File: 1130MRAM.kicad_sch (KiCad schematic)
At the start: 123 parts, among them J1 Screw_Terminal_01x03, J1A09 SLTpad, J1A11 SLTpad, K1E09 SLTpad, K1E11 SLTpad, M1A09 SLTpad, M1A11 SLTpad, M1C09 SLTpad, M1D09 SLTpad, M1E09 SLTpad, M1E11 SLTpad, Q1 IRF540N, SW1 SLTpad, U1 MR0A16AYS35, U10 74LCX38, U11 74LCX38, U12 SN74LVC1G123DCUR, U13 SN74LVC1G123DCUR, U14 74HC00, U15 74LS86, U16 74LS86, U17 74LS86, U18 74LS86, U2 SN74LV240APWR, U3 SN74LV240APWR, U4 LDL1117, U5 SN74LVC1G123DCUR, U6 SN74LVC1G123DCUR, U7 74LCX38, U8 74LCX38, U9 74LCX38

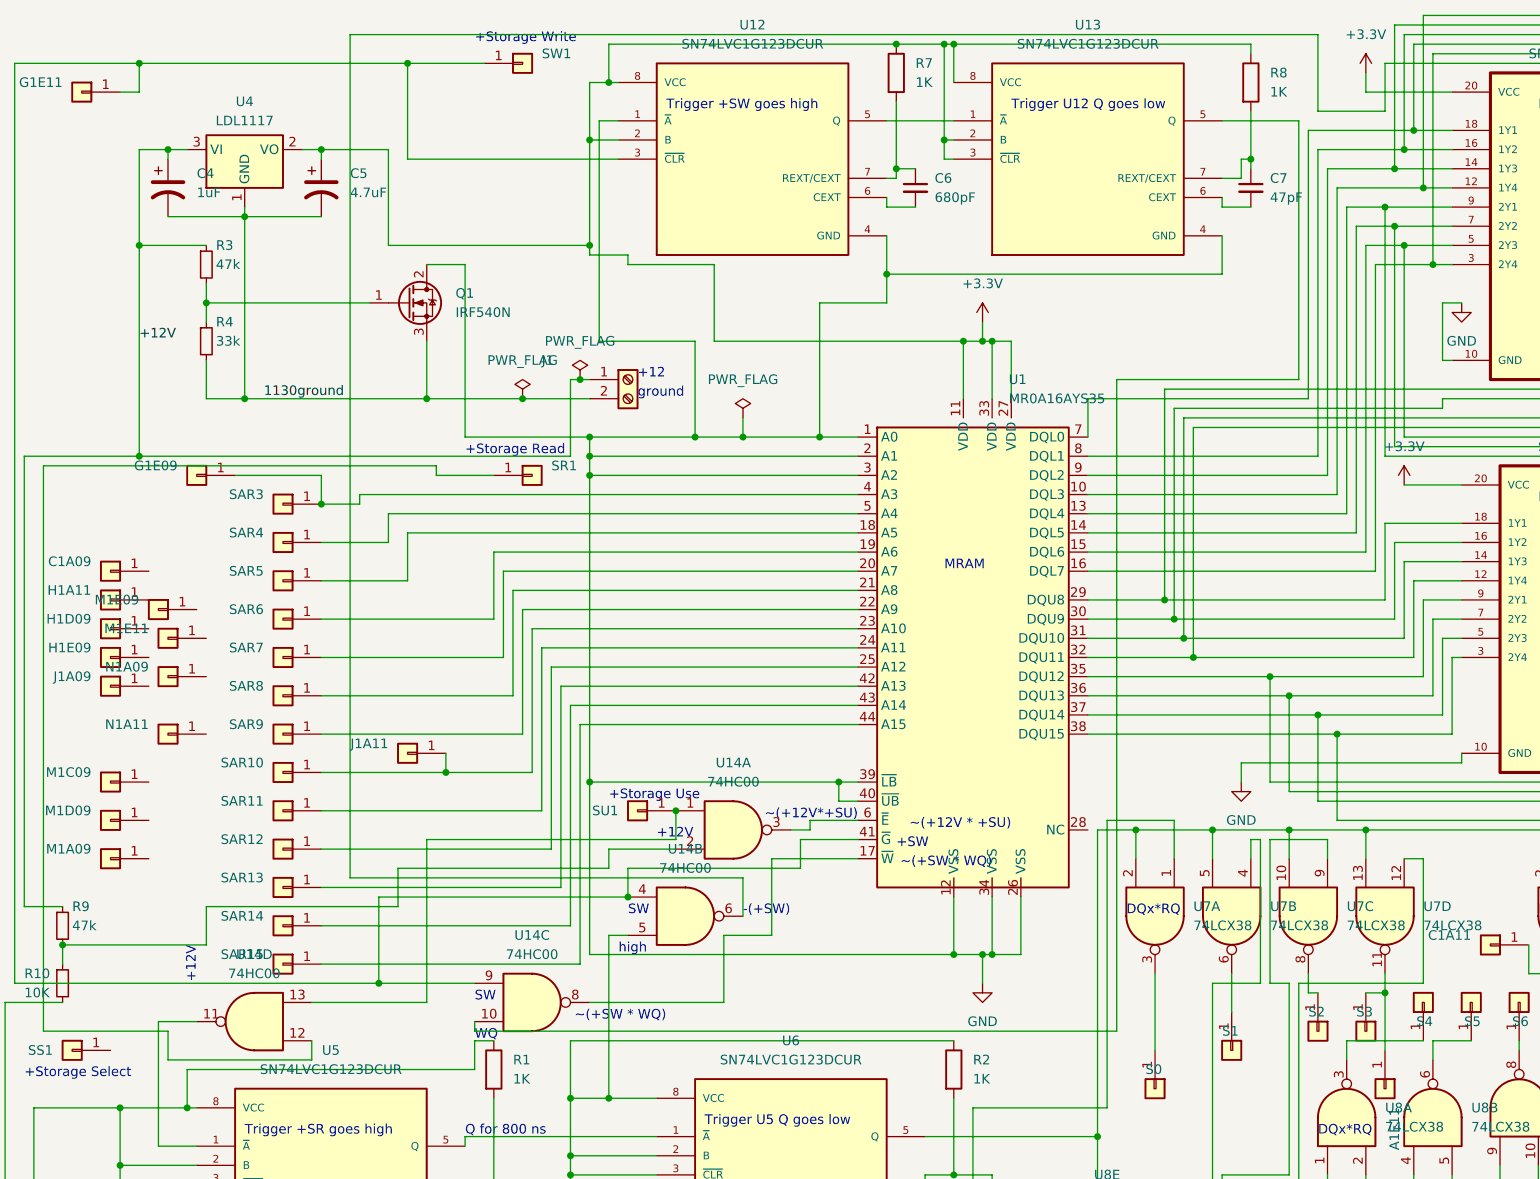
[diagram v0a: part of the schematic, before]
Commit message: Newest version of the PCB
based on testing with the 1130, the PCB was modified substantially
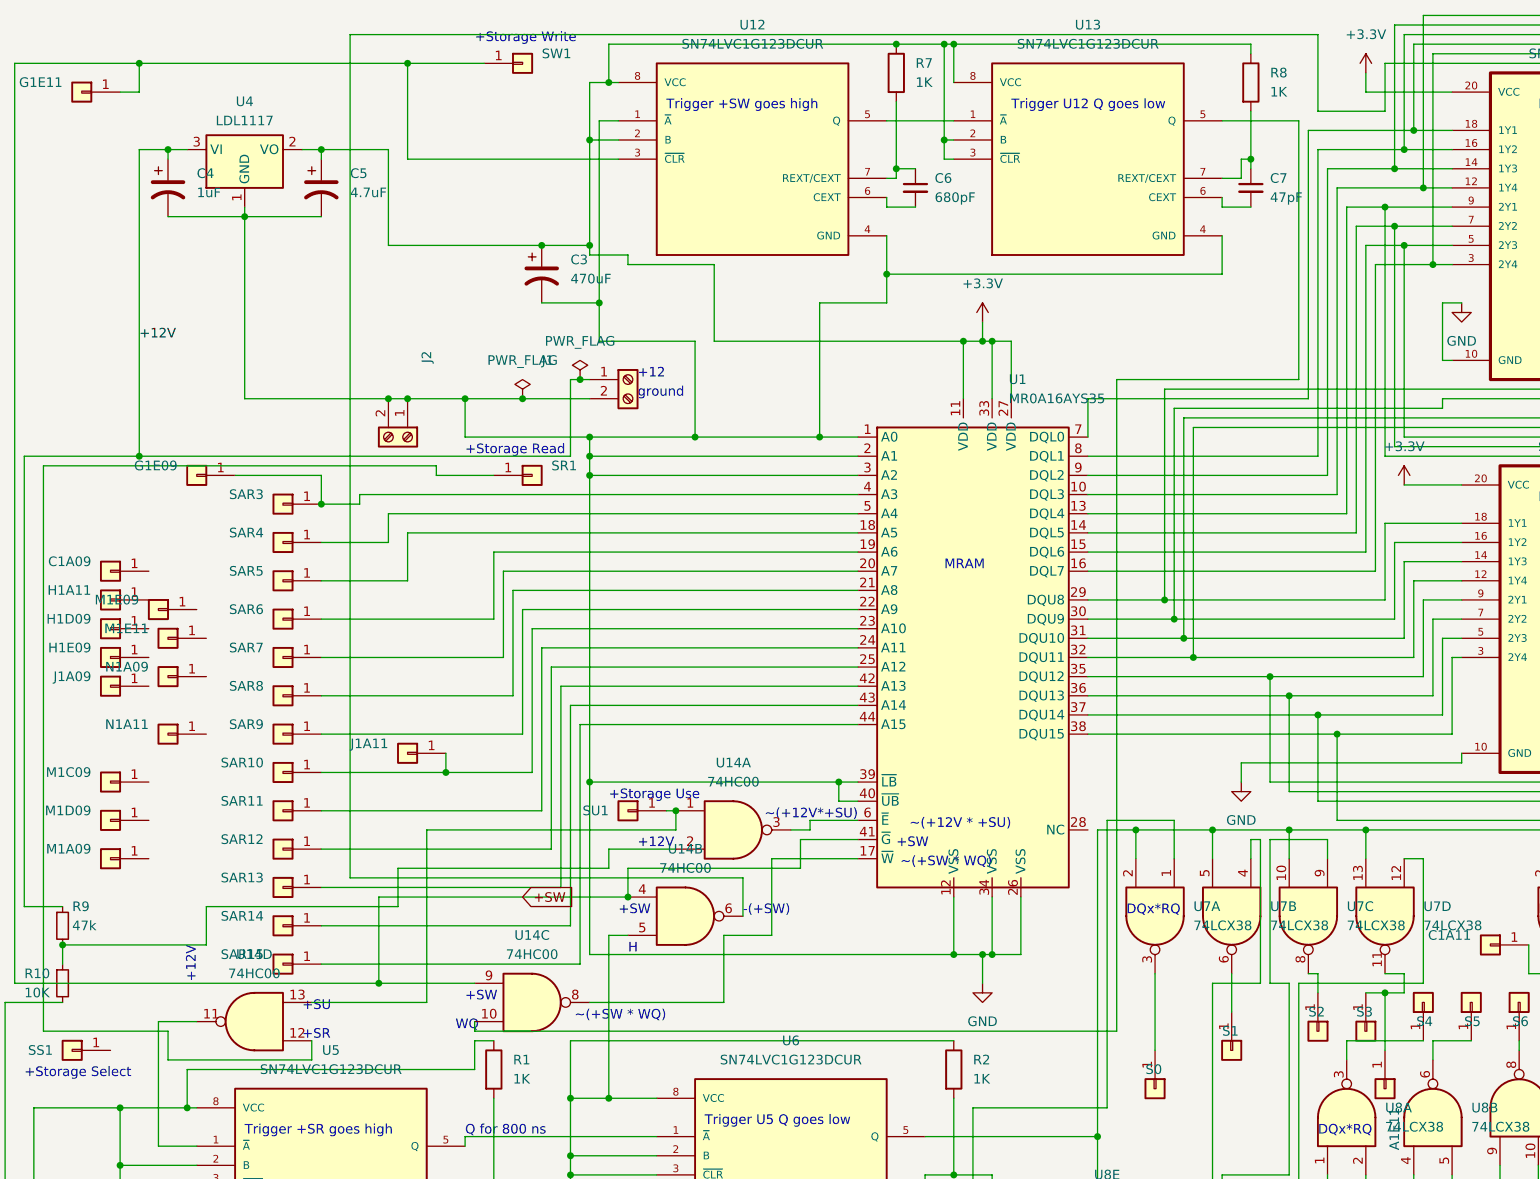
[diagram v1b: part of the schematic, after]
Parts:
- removed Q1: IRF540N, Package_TO_SOT_SMD:TO-263-2, symbol Transistor_FET:IRF540N
- removed R3: 47k, Resistor_SMD:R_0805_2012Metric, symbol Device:R_Small
- removed R4: 33k, Resistor_SMD:R_0805_2012Metric, symbol Device:R_Small
- added C3: 470uF, Capacitor_Tantalum_SMD:CP_EIA-7343-30_AVX-N, symbol Device:C_Polarized_US
- added J2: Screw_Terminal_01x03, Connector_Phoenix_MC_HighVoltage:PhoenixContact_MCV_1,5_2-G-5.08_1x02_P5.08mm_Vertical, symbol Connector:Screw_Terminal_01x02
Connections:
- net 1130ground is gone; now on net GND: C4.2, C5.2, J1.2 (Pin_2), U4.1 (GND)
- net +3.3V: now also C3.1
- net GND: now also C3.2, J2.1 (Pin_1), J2.2 (Pin_2)
- net +SW: now reaches G1E11.1 (Pin_1), SW1.1 (Pin_1), U1.41 (~{G}), U12.3 (~{CLR}), U14.4, U14.9
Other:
- note added: "+SR"
- note added: "+SU"
- note added: "H"
- note removed: "SW"
- note removed: "high"
- moved on the sheet: SU1

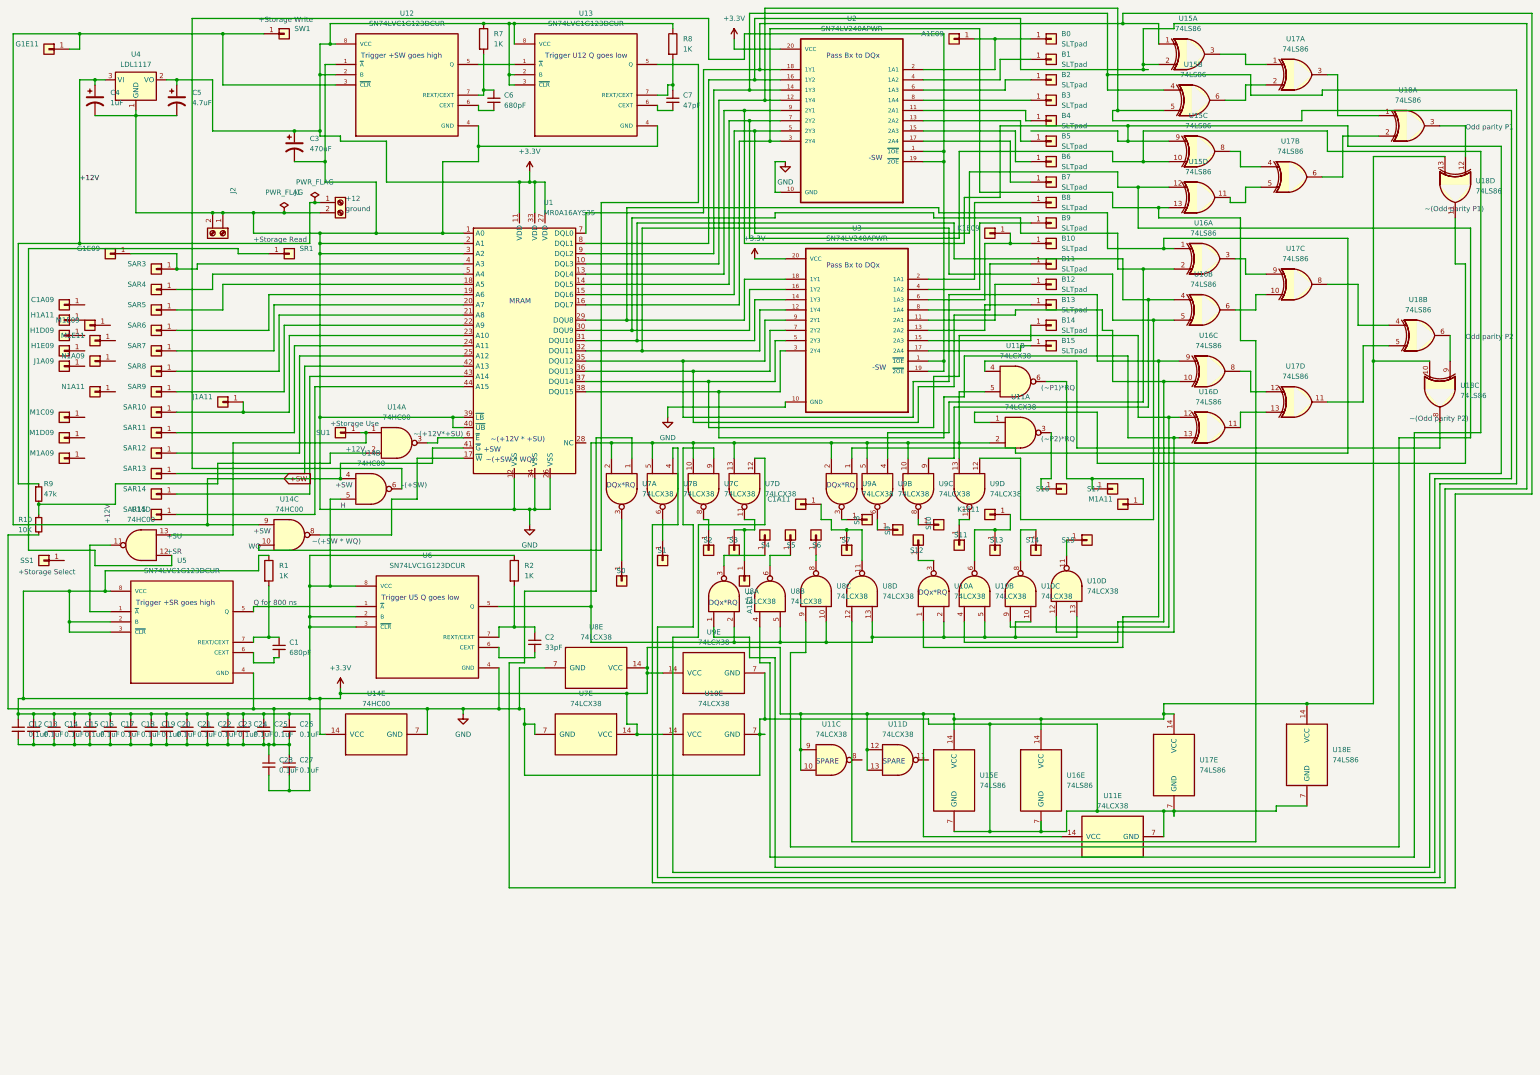
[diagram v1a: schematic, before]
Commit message: Changes after testing
tweaks to design, components, and documentation.
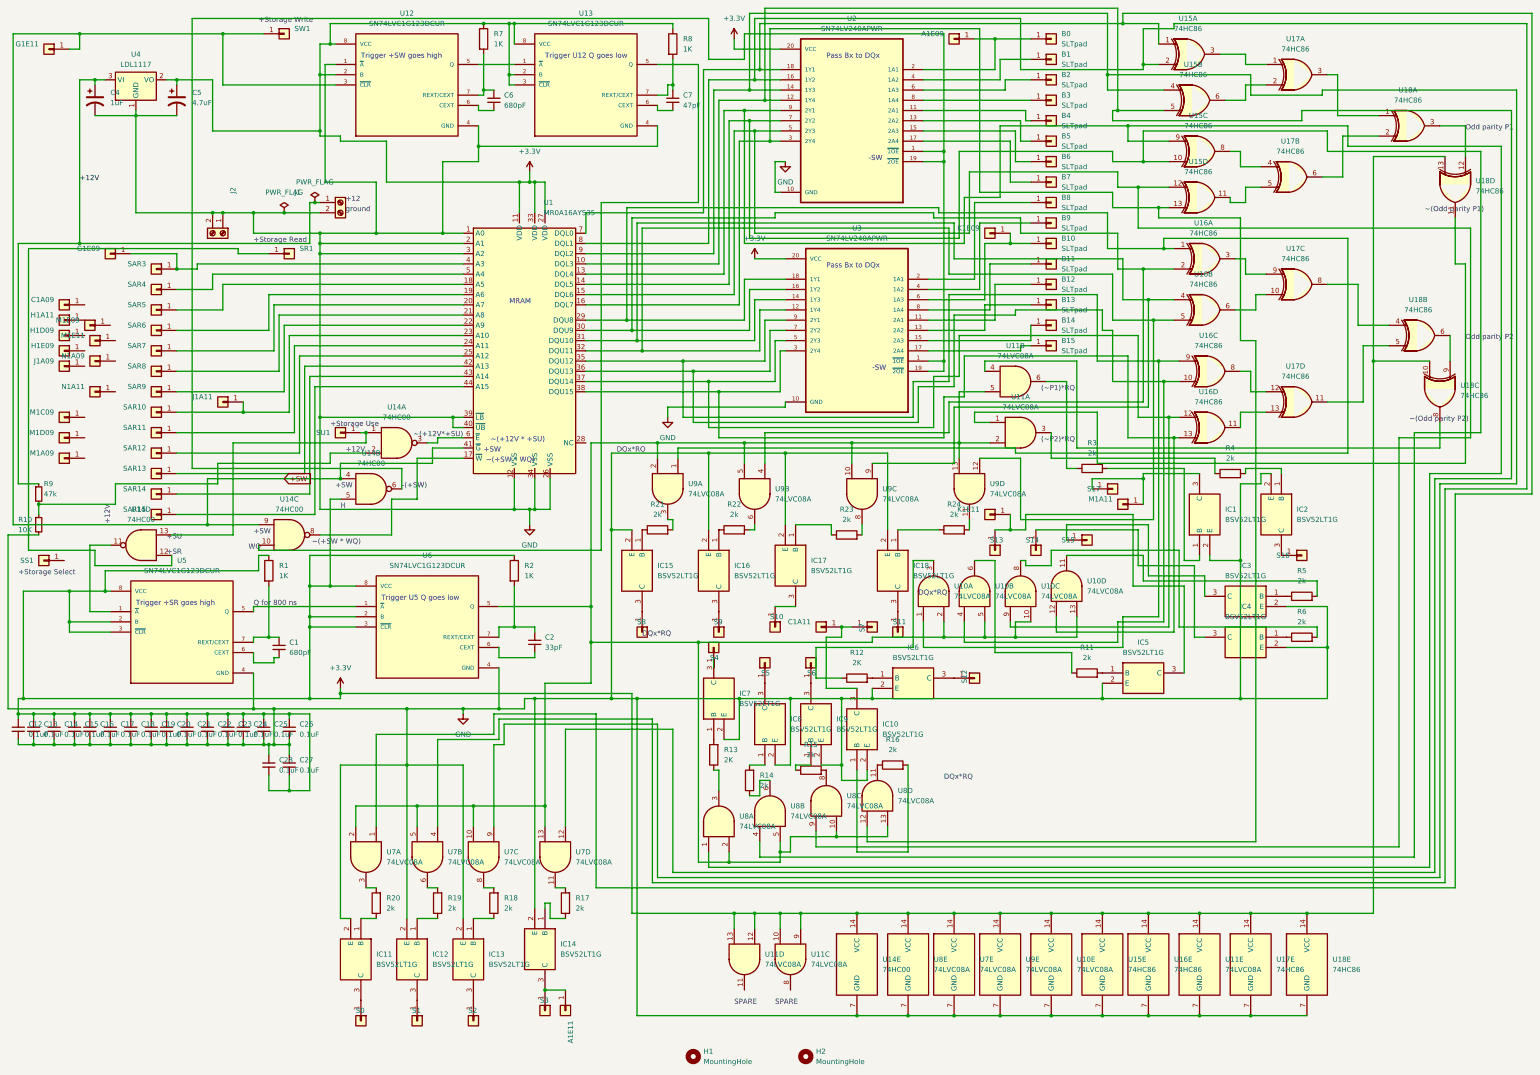
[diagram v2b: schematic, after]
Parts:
- removed C3: 470uF, Capacitor_Tantalum_SMD:CP_EIA-7343-30_AVX-N, symbol Device:C_Polarized_US
- added H1, H2: MountingHole, MountingHole:MountingHole_4.3mm_M4, symbol Mechanical:MountingHole
- added IC1, IC10, IC11, IC12, IC13, IC14, IC15, IC16, IC17, IC18, IC2, IC3, IC4, IC5, IC6, IC7, IC8, IC9: BSV52LT1G, SamacSys_Parts:SOT95P237X111-3N, symbol SamacSys_Parts:BSV52LT1G
- added R11, R14, R15, R16, R17, R18, R19, R20, R21, R22, R23, R24, R3, R4, R5, R6: 2k, Resistor_SMD:R_0805_2012Metric, symbol Device:R
- added R12, R13: 2K, Resistor_SMD:R_0805_2012Metric, symbol Device:R
- U10, U11, U7, U8, U9: value 74LCX38 -> 74LVC08A; symbol 74xx:74LS03 -> 74xx:74LS08
- U15, U16, U17, U18: value 74LS86 -> 74HC86
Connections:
- net GND: now also IC1.2 (E), IC10.2 (E), IC11.2 (E), IC12.2 (E), IC13.2 (E), IC14.2 (E), IC15.2 (E), IC16.2 (E), IC17.2 (E), IC18.2 (E), IC2.2 (E), IC3.2 (E), IC4.2 (E), IC5.2 (E), IC6.2 (E), IC7.2 (E), IC8.2 (E), IC9.2 (E)
- net at K1E11.1 (Pin_1), S13.1 (Pin_1): now also IC5.3 (C); no longer U10.6
- net at C1A11.1 (Pin_1), S7.1 (Pin_1): now also IC10.3 (C); no longer U8.11
- net at S9.1 (Pin_1): now also IC16.3 (C); no longer U9.6
- net at M1A11.1 (Pin_1), S17.1 (Pin_1): now also IC1.3 (C); no longer U11.6
- net at U10.11: now also R5.2; no longer S15.1 (Pin_1)
- net at S8.1 (Pin_1): now also IC15.3 (C); no longer U9.3
- net at S4.1 (Pin_1): now also IC7.3 (C); no longer U8.3
- net at S10.1 (Pin_1): now also IC17.3 (C); no longer U9.8
- net at U7.3: now also R20.2; no longer S0.1 (Pin_1)
- net at U7.8: now also R18.2; no longer S2.1 (Pin_1)
- net at S16.1 (Pin_1): now also IC2.3 (C); no longer U11.3
- net at S14.1 (Pin_1): now also IC4.3 (C); no longer U10.8
- net at S6.1 (Pin_1): now also IC9.3 (C); no longer U8.8
- net at U10.3: now also R12.1; no longer S12.1 (Pin_1)
- net at A1E11.1 (Pin_1), S3.1 (Pin_1): now also IC14.3 (C); no longer U7.11
- net at U9.11: now also R24.2; no longer S11.1 (Pin_1)
- net at U7.6: now also R19.2; no longer S1.1 (Pin_1)
- net at U8.6: now also R14.1; no longer S5.1 (Pin_1)
- new net: IC10.1 (B), R16.2
- new net: IC14.1 (B), R17.1
- new net: R17.2, U7.11
- new net: R11.1, U10.6
- new net: IC15.1 (B), R21.1
- new net: IC16.1 (B), R22.1
- new net: R16.1, U8.11
- new net: IC4.1 (B), R6.1
- new net: R22.2, U9.6
- new net: IC3.1 (B), R5.1
- new net: R21.2, U9.3
- new net: IC8.1 (B), R14.2
- new net: IC12.1 (B), R19.1
- new net: IC13.1 (B), R18.1
- new net: IC11.1 (B), R20.1
- new net: R3.1, U11.6
- new net: IC1.1 (B), R3.2
- new net: IC7.1 (B), R13.2
- new net: IC2.1 (B), R4.2
- new net: IC9.1 (B), R15.1
- new net: IC8.3 (C), S5.1 (Pin_1)
- new net: IC11.3 (C), S0.1 (Pin_1)
- new net: R4.1, U11.3
- new net: IC17.1 (B), R23.1
- new net: R23.2, U9.8
- new net: IC18.1 (B), R24.1
- new net: IC12.3 (C), S1.1 (Pin_1)
- new net: IC13.3 (C), S2.1 (Pin_1)
- new net: IC3.3 (C), S15.1 (Pin_1)
- new net: R13.1, U8.3
- new net: IC6.1 (B), R12.2
- new net: IC5.1 (B), R11.2
- new net: IC6.3 (C), S12.1 (Pin_1)
- new net: R6.2, U10.8
- new net: R15.2, U8.8
- new net: IC18.3 (C), S11.1 (Pin_1)
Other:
- moved on the sheet: A1E11, C1A11, S0, S1, S10, S11, S12, S16, S2, S3, S4, S5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
